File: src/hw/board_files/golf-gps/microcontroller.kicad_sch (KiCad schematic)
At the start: 25 parts, among them SW2 BTN_1, SW3 BTN_2, SW4 RESET, SW5 BTN_3, U4 STM32L432KCU6, Y1 32.768kHz

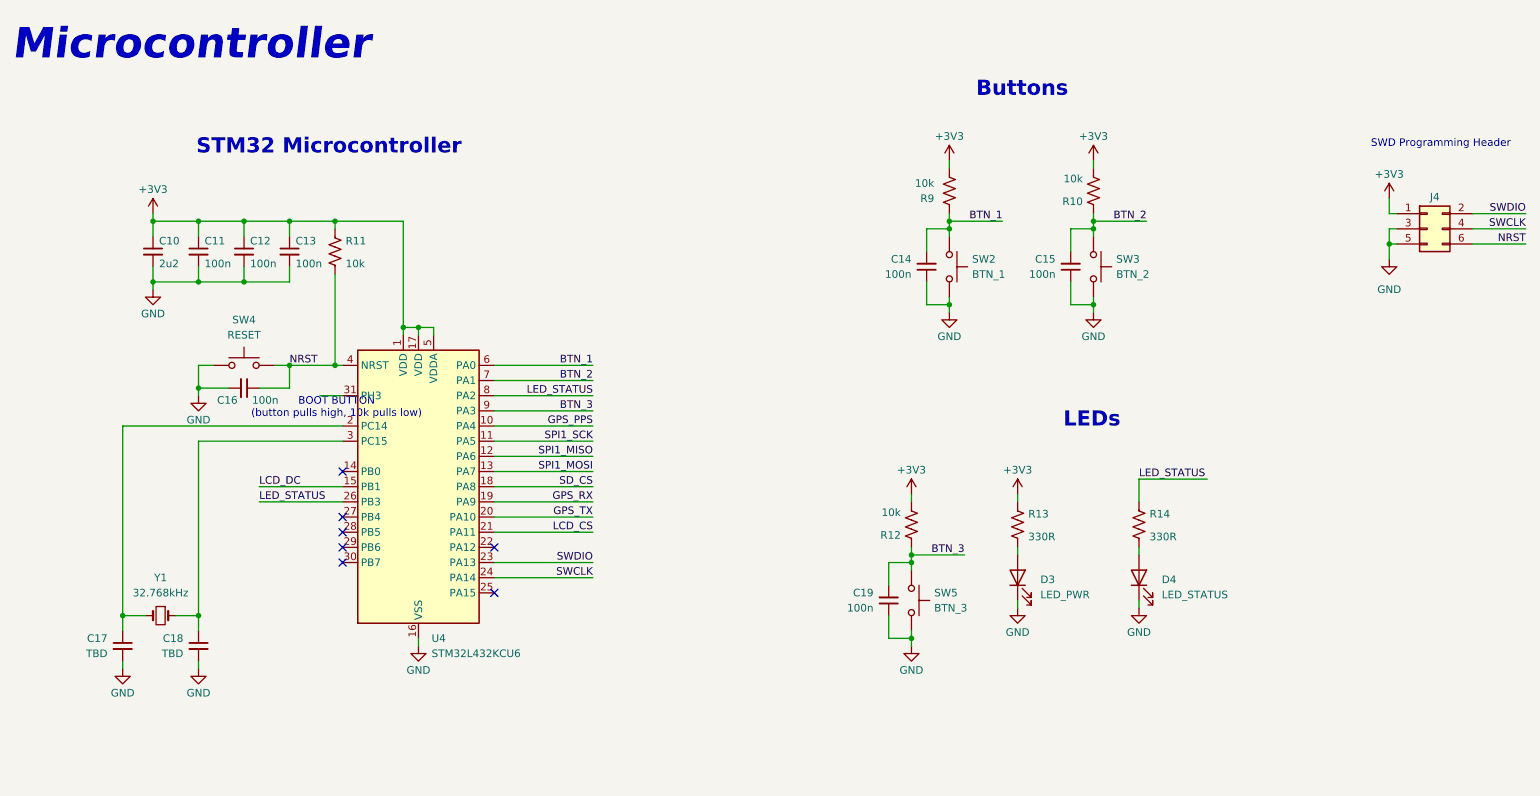
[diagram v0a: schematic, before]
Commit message: Added PI filter to antenna.
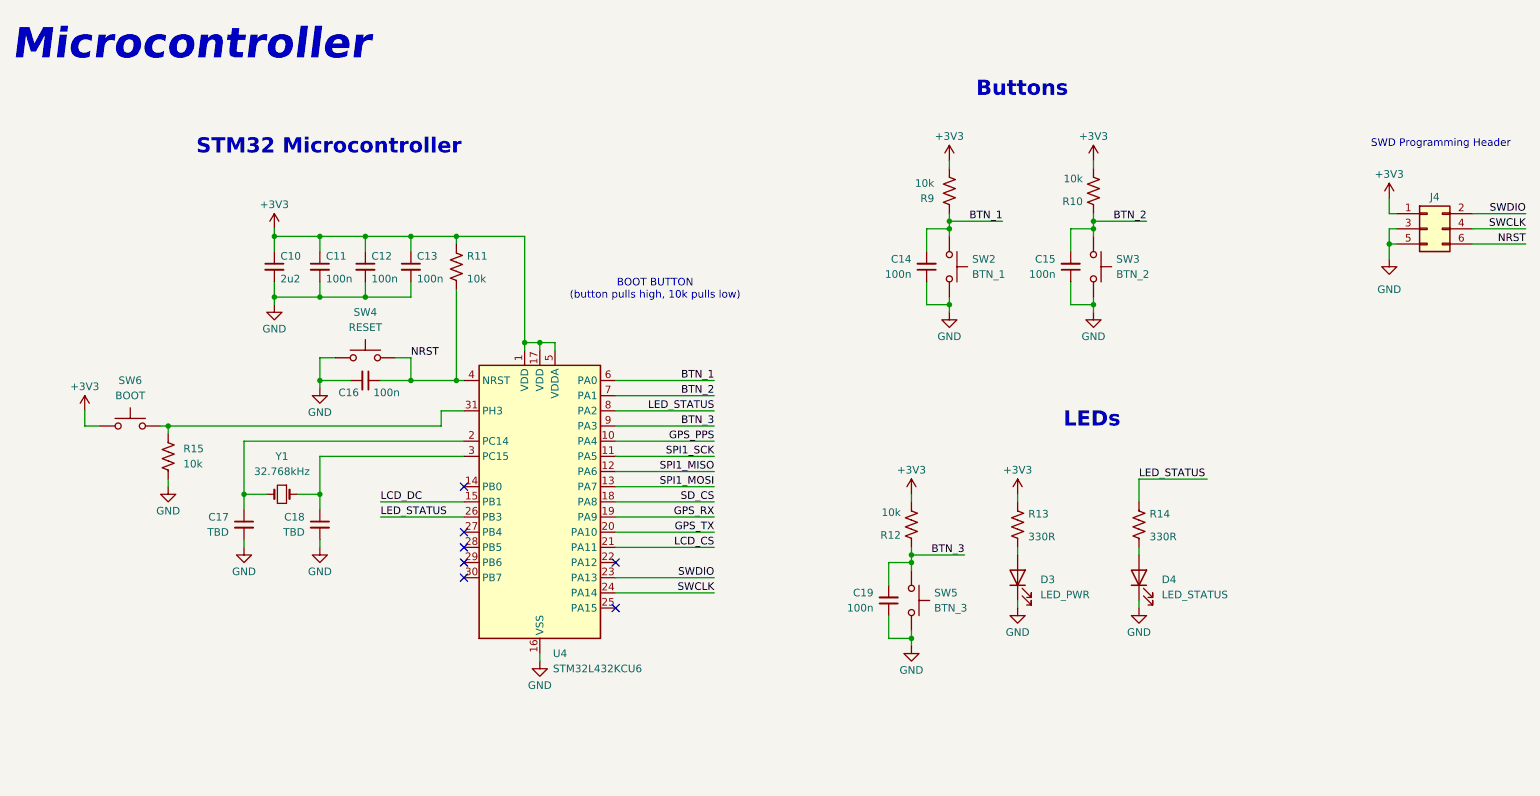
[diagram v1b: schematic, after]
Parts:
- added R15: 10k, symbol Device:R_US
- added SW6: BOOT, symbol Switch:SW_Push
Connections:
- net +3V3: now also SW6.1
- net GND: now also R15.2
- net at U4.31 (PH3): now also R15.1, SW6.2
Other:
- moved on the sheet: C10, C11, C12, C13, C16, C17, C18, R11, SW4, U4, Y1

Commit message: Finished sch, started power section on PCB
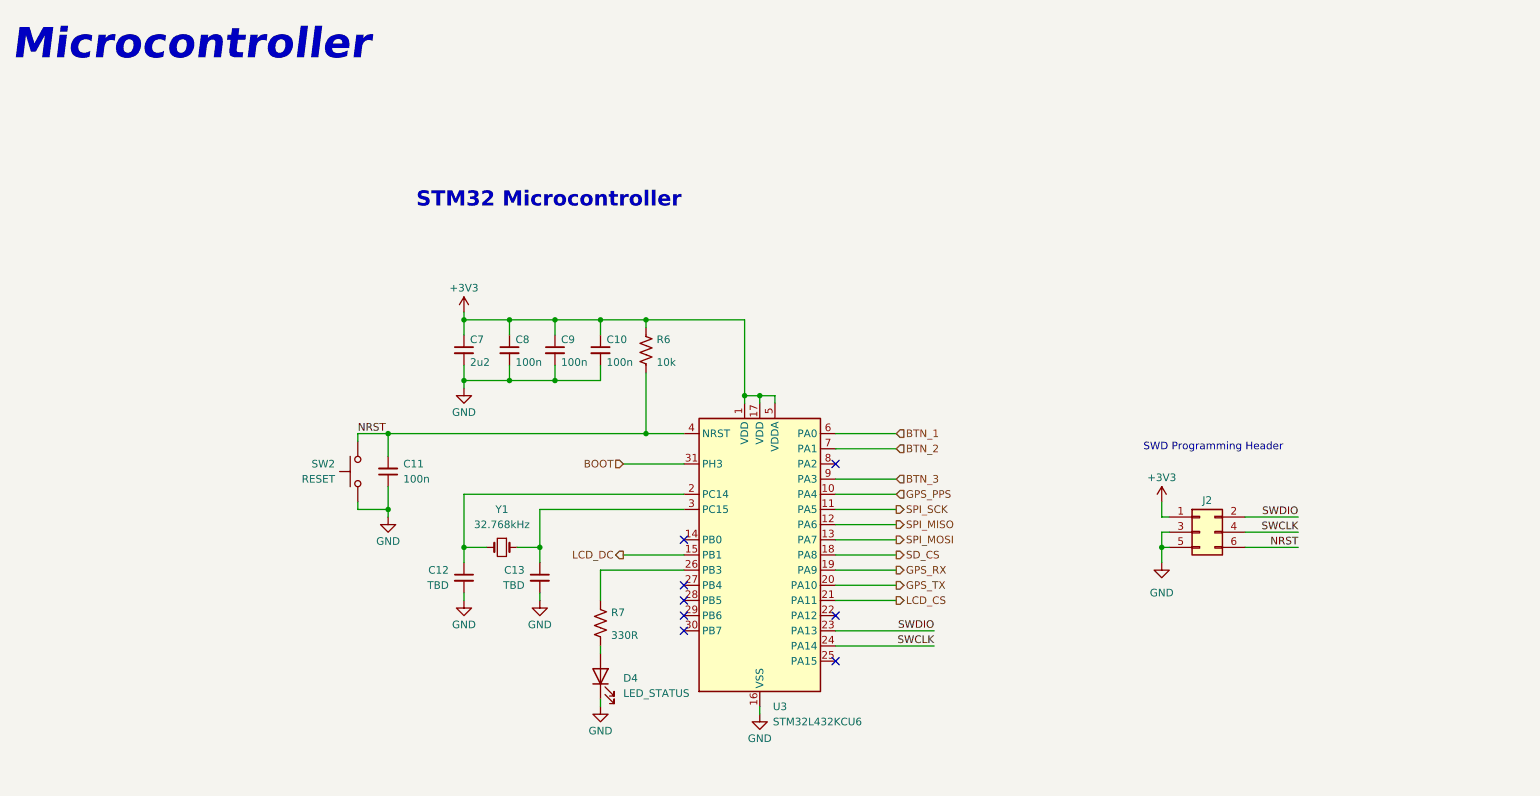
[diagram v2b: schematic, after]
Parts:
- removed C14, C15, C19: 100n, symbol Device:C_Small
- removed D3: LED_PWR, symbol Device:LED
- removed R10, R12, R15, R9: 10k, symbol Device:R_US
- removed R13: 330R, symbol Device:R_US
- removed SW2: BTN_1, symbol Switch:SW_Push
- removed SW3: BTN_2, symbol Switch:SW_Push
- removed SW5: BTN_3, symbol Switch:SW_Push
- removed SW6: BOOT, symbol Switch:SW_Push
- C10: renamed from C13; footprint (none) -> Capacitor_SMD:C_0603_1608Metric
- C11: renamed from C16; footprint (none) -> Capacitor_SMD:C_0603_1608Metric
- C12: renamed from C17; footprint (none) -> Capacitor_SMD:C_0603_1608Metric
- C13: renamed from C18; footprint (none) -> Capacitor_SMD:C_0603_1608Metric
- C7: renamed from C10; footprint (none) -> Capacitor_SMD:C_0603_1608Metric
- C8: renamed from C11; footprint (none) -> Capacitor_SMD:C_0603_1608Metric
- C9: renamed from C12; footprint (none) -> Capacitor_SMD:C_0603_1608Metric
- D4: footprint (none) -> LED_SMD:LED_0805_2012Metric
- R6: renamed from R11; footprint (none) -> Resistor_SMD:R_0603_1608Metric
- R7: renamed from R14; footprint (none) -> Resistor_SMD:R_0603_1608Metric
- SW2: renamed from SW4; footprint (none) -> Button_Switch_THT:SW_PUSH_6mm_H4.3mm
- Y1: footprint (none) -> Crystal:Crystal_DS26_D2.0mm_L6.0mm_Horizontal
- renumbered J4 to J2, U4 to U3
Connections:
- net GND: now also C11.1, SW2.2; no longer C11.2, SW2.1
- net NRST: now also C11.2, SW2.1; no longer C11.1, SW2.2
- net BOOT: now reaches U3.31 (PH3)
- net LED_STATUS: no longer names the net of R7.1, U3.26 (PB3)
- net LED_STATUS: no longer U3.8 (PA2)
- net SPI1_MISO renamed SPI_MISO
- net SPI1_MOSI renamed SPI_MOSI
- net SPI1_SCK renamed SPI_SCK
- no-connect marks 7 -> 8
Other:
- note removed: "BOOT BUTTON (button pulls high, 10k pulls low)"
- note removed: "Buttons"
- note removed: "LEDs"
- company: Brady Kuhn -> B. Kuhn
- moved on the sheet: C10, C11, C12, C13, C7, C8, C9, D4, J2, R6, R7, SW2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

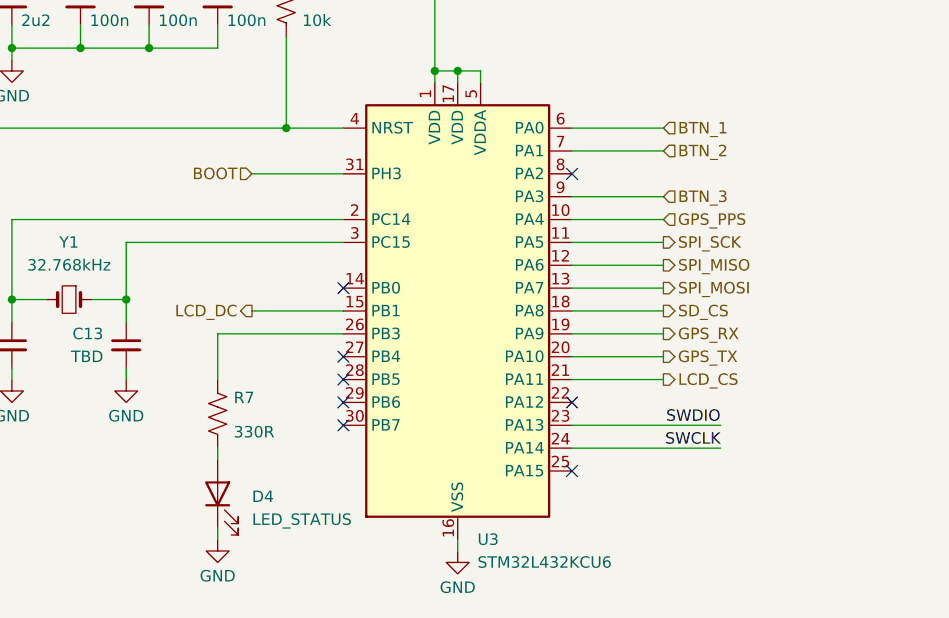
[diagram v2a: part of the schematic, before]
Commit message: Added USBC to UART bridge for programming. Changed pinout. Added pinout spreadsheet in docs.
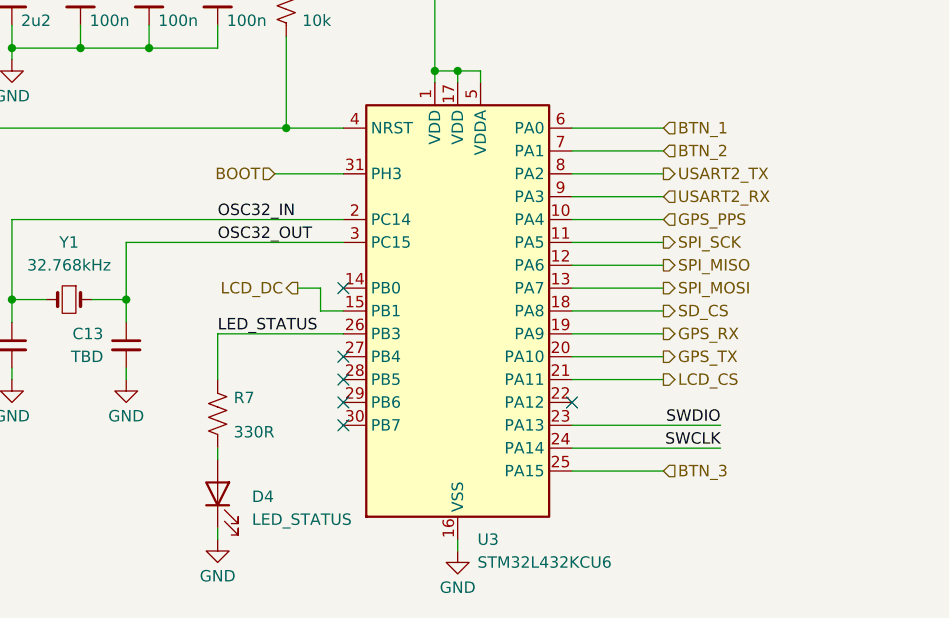
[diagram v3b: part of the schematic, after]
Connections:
- net BTN_3: now also U3.25 (PA15); no longer U3.9 (PA3)
- net LED_STATUS: now reaches R7.1, U3.26 (PB3)
- net OSC32_OUT: now reaches C13.1, U3.3 (PC15), Y1.1
- net OSC32_IN: now reaches C12.1, U3.2 (PC14), Y1.2
- net USART2_TX: now reaches U3.8 (PA2)
- new net USART2_RX: U3.9 (PA3)
- no-connect marks 8 -> 6
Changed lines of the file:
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@@
-	)
-	(no_connect
-		(at 152.4 121.92)
-	)
-	(no_connect
-		(at 152.4 88.9)
 	)
 	(no_connect
@@
 	(wire
 		(pts
+			(xy 121.92 101.6) (xy 124.46 101.6)
+		)
+		(stroke
+			(width 0)
+			(type default)
+		)
+	)
+	(wire
+		(pts
 			(xy 113.03 119.38) (xy 113.03 120.65)
 		)
@@
 	(wire
 		(pts
+			(xy 152.4 88.9) (xy 162.56 88.9)
+		)
+		(stroke
+			(width 0)
+			(type default)
+		)
+	)
+	(wire
+		(pts
 			(xy 105.41 72.39) (xy 105.41 74.93)
 		)
@@
 	(wire
 		(pts
-			(xy 116.84 88.9) (xy 127 88.9)
+			(xy 119.38 88.9) (xy 127 88.9)
 		)
 		(stroke
@@
 	(wire
 		(pts
+			(xy 124.46 104.14) (xy 124.46 101.6)
+		)
+		(stroke
+			(width 0)
+			(type default)
+		)
+	)
+	(wire
+		(pts
 			(xy 113.03 128.27) (xy 113.03 129.54)
 		)
@@
 	(wire
 		(pts
+			(xy 127 104.14) (xy 124.46 104.14)
+		)
+		(stroke
+			(width 0)
+			(type default)
+		)
+	)
+	(wire
+		(pts
 			(xy 97.79 72.39) (xy 97.79 74.93)
 		)
@@
 	(wire
 		(pts
+			(xy 152.4 91.44) (xy 162.56 91.44)
+		)
+		(stroke
+			(width 0)
+			(type default)
+		)
+	)
+	(wire
+		(pts
 			(xy 137.16 64.77) (xy 137.16 77.47)
 		)
@@
 	(wire
 		(pts
-			(xy 152.4 91.44) (xy 162.56 91.44)
+			(xy 152.4 121.92) (xy 162.56 121.92)
 		)
 		(stroke
@@
 		(pts
 			(xy 207.01 102.87) (xy 207.01 105.41)
-		)
-		(stroke
-			(width 0)
-			(type default)
-		)
-	)
-	(wire
-		(pts
-			(xy 116.84 104.14) (xy 127 104.14)
 		)
 		(stroke
@@
 		)
 	)
+	(label "LED_STATUS"
+		(at 113.03 106.68 0)
+		(fields_autoplaced yes)
+		(effects
+			(font
+				(size 1.27 1.27)
+			)
+			(justify left bottom)
+		)
+	)
 	(label "SWDIO"
 		(at 229.87 97.79 180)
@@
 		)
 	)
+	(label "OSC32_OUT"
+		(at 113.03 96.52 0)
+		(fields_autoplaced yes)
+		(effects
+			(font
+				(size 1.27 1.27)
+			)
+			(justify left bottom)
+		)
+	)
 	(label "SWDIO"
 		(at 168.91 116.84 180)
@@
 		)
 	)
+	(label "OSC32_IN"
+		(at 113.03 93.98 0)
+		(fields_autoplaced yes)
+		(effects
+			(font
+				(size 1.27 1.27)
+			)
+			(justify left bottom)
+		)
+	)
 	(label "NRST"
 		(at 72.39 83.82 0)
@@
 			)
 			(justify right bottom)
+		)
+	)
+	(hierarchical_label "USART2_TX"
+		(shape output)
+		(at 162.56 88.9 0)
+		(fields_autoplaced yes)
+		(effects
+			(font
+				(size 1.27 1.27)
+			)
+			(justify left)
 		)
 	)
@@
 		)
 	)
+	(hierarchical_label "USART2_RX"
+		(shape input)
+		(at 162.56 91.44 0)
+		(fields_autoplaced yes)
+		(effects
+			(font
+				(size 1.27 1.27)
+			)
+			(justify left)
+		)
+	)
 	(hierarchical_label "SD_CS"
 		(shape output)
@@
 	(hierarchical_label "BTN_3"
 		(shape input)
-		(at 162.56 91.44 0)
+		(at 162.56 121.92 0)
 		(fields_autoplaced yes)
 		(effects
@@
 	(hierarchical_label "LCD_DC"
 		(shape output)
-		(at 116.84 104.14 180)
+		(at 121.92 101.6 180)
 		(fields_autoplaced yes)
 		(effects
@@
 	(hierarchical_label "BOOT"
 		(shape input)
-		(at 116.84 88.9 180)
-		(fields_autoplaced yes)
-		(effects
+		(at 119.38 88.9 180)
+		(fields_autoplaced yes)
+		(effects

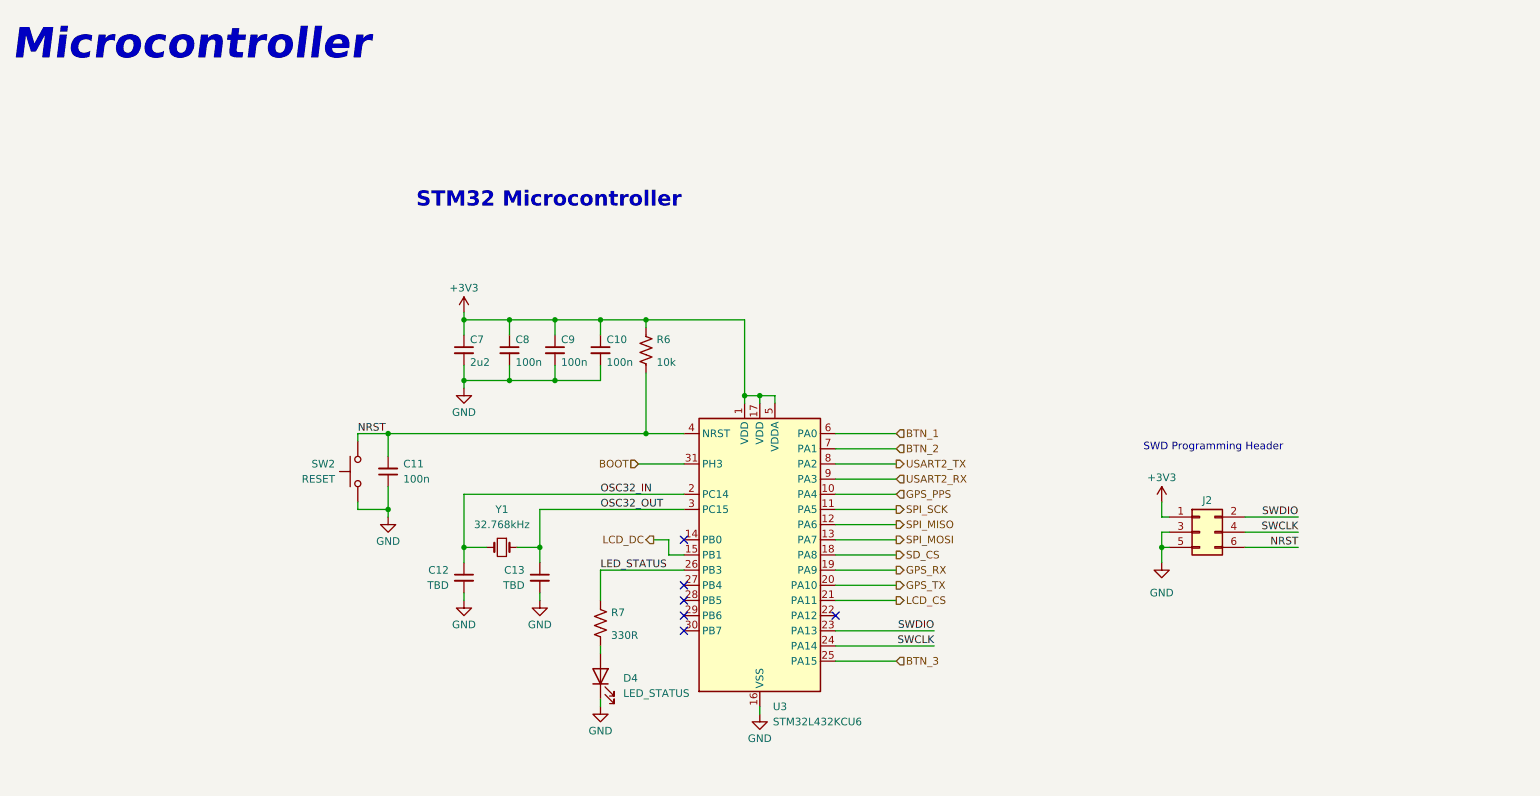
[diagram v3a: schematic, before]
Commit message: Finished new sch. Updated pinout. Started new PCB.
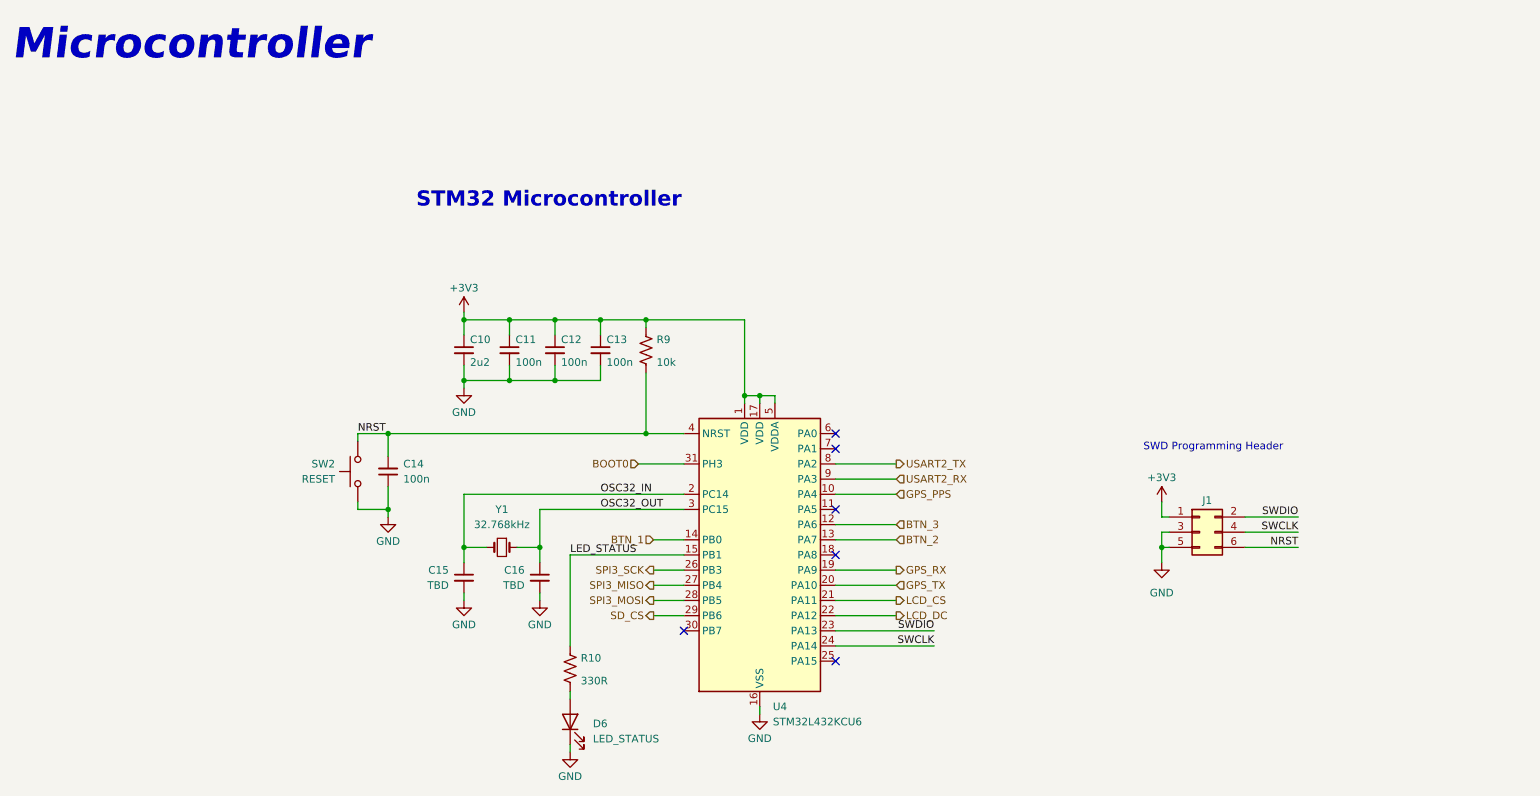
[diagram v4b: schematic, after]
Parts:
- renumbered C7 to C10, C8 to C11, C9 to C12, C10 to C13, C11 to C14, C12 to C15, C13 to C16, D4 to D6, J2 to J1, R7 to R10, R6 to R9, U3 to U4
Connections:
- net SPI_MISO is gone; now on net BTN_3: U4.12 (PA6)
- net SPI_MOSI is gone; now on net BTN_2: U4.13 (PA7)
- net BTN_1: now also U4.14 (PB0); no longer U4.6 (PA0)
- net BTN_2: no longer U4.7 (PA1)
- net BTN_3: no longer U4.25 (PA15)
- net LCD_DC: now also U4.22 (PA12); no longer U4.15 (PB1)
- net LED_STATUS: now also U4.15 (PB1); no longer U4.26 (PB3)
- net SD_CS: now also U4.29 (PB6); no longer U4.18 (PA8)
- net SPI3_MISO: now reaches U4.27 (PB4)
- net SPI3_MOSI: now reaches U4.28 (PB5)
- net BOOT renamed BOOT0
- net SPI_SCK: no longer names the net of U4.11 (PA5)
- new net SPI3_SCK: U4.26 (PB3)
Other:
- moved on the sheet: D6, R10
